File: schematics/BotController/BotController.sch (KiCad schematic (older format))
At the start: 53 parts, among them IC1 ATMEGA644A-P, P1 2x Serial, P10 Stepper Upperarm, P11 Stepper Shoulder, P12 POWER_IN, P13 PowerEnableIn, P17 PowerEnableOut, P2 Herkulex Servo, P28 Power Stepper, P3 Encoder Socket 0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

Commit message: resorted
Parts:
- added C?: 100nF, symbol C
- C11: value 100uF -> 2200uF
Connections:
- wire segments 217 -> 290
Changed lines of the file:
@@
 P 4750 10450
 F 0 "C11" H 4775 10550 50  0000 L CNN
-F 1 "100uF" H 4775 10350 50  0000 L CNN
+F 1 "2200uF" H 4775 10350 50  0000 L CNN
 F 2 "Capacitors_ThroughHole:C_Radial_D7.5_L11.2_P2.5" H 4788 10300 50  0001 C CNN
 F 3 "" H 4750 10450 50  0000 C CNN
@@
 	2250 7150 2250 7350
 Wire Wire Line
-	1000 7150 2250 7150
+	1000 7150 2050 7150
+Wire Wire Line
+	2050 7150 2250 7150
 Wire Wire Line
 	2050 7800 2050 7650
@@
 Connection ~ 2050 7150
 Wire Wire Line
-	9900 2700 9900 6350
+	9900 2700 9900 6200
+Wire Wire Line
+	9900 6200 9900 6350
 Wire Wire Line
 	9400 1700 9400 4000
@@
 Connection ~ 3050 1700
 Wire Wire Line
-	3050 1700 3050 7300
+	3050 1700 3050 7150
+Wire Wire Line
+	3050 7150 3050 7300
 Connection ~ 2250 7800
 Connection ~ 2050 7800
 Wire Wire Line
-	950  7800 3900 7800
+	950  7800 1200 7800
+Wire Wire Line
+	1200 7800 1750 7800
+Wire Wire Line
+	1750 7800 2050 7800
+Wire Wire Line
+	2050 7800 2250 7800
+Wire Wire Line
+	2250 7800 2650 7800
+Wire Wire Line
+	2650 7800 3050 7800
+Wire Wire Line
+	3050 7800 3900 7800
 Wire Wire Line
 	7350 6200 7350 6550
@@
 	9400 6200 9400 4300
 Wire Wire Line
-	6050 4200 9400 4200
-Wire Wire Line
-	6050 4100 9400 4100
+	6050 4200 8500 4200
+Wire Wire Line
+	8500 4200 9150 4200
+Wire Wire Line
+	9150 4200 9400 4200
+Wire Wire Line
+	6050 4100 8400 4100
+Wire Wire Line
+	8400 4100 8950 4100
+Wire Wire Line
+	8950 4100 9400 4100
 Wire Wire Line
 	7050 5300 7050 6550
@@
 	3700 6200 3700 5000
 Wire Wire Line
-	3700 1700 3700 4500
+	3700 1700 3700 3500
+Wire Wire Line
+	3700 3500 3700 4500
 Wire Wire Line
 	4050 3500 3700 3500
@@
 	6350 6200 6350 6550
 Wire Wire Line
-	1200 6200 11750 6200
+	1200 6200 1700 6200
+Wire Wire Line
+	1700 6200 2150 6200
+Wire Wire Line
+	2150 6200 2750 6200
+Wire Wire Line
+	2750 6200 3450 6200
+Wire Wire Line
+	3450 6200 3700 6200
+Wire Wire Line
+	3700 6200 4850 6200
+Wire Wire Line
+	4850 6200 5050 6200
+Wire Wire Line
+	5050 6200 6350 6200
+Wire Wire Line
+	6350 6200 7350 6200
+Wire Wire Line
+	7350 6200 8150 6200
+Wire Wire Line
+	8150 6200 9400 6200
+Wire Wire Line
+	9400 6200 9900 6200
+Wire Wire Line
+	9900 6200 10300 6200
+Wire Wire Line
+	10300 6200 10800 6200
+Wire Wire Line
+	10800 6200 11300 6200
+Wire Wire Line
+	11300 6200 11750 6200
 Wire Wire Line
 	7500 3900 6050 3900
@@
 	8150 4550 7850 4550
 Wire Wire Line
-	1200 1700 9400 1700
-Wire Wire Line
-	2750 2300 4050 2300
+	1200 1700 1700 1700
+Wire Wire Line
+	1700 1700 3050 1700
+Wire Wire Line
+	3050 1700 3450 1700
+Wire Wire Line
+	3450 1700 3700 1700
+Wire Wire Line
+	3700 1700 3850 1700
+Wire Wire Line
+	3850 1700 4050 1700
+Wire Wire Line
+	4050 1700 4850 1700
+Wire Wire Line
+	4850 1700 5050 1700
+Wire Wire Line
+	5050 1700 7050 1700
+Wire Wire Line
+	7050 1700 7850 1700
+Wire Wire Line
+	7850 1700 9150 1700
+Wire Wire Line
+	9150 1700 9400 1700
+Wire Wire Line
+	2750 2300 3850 2300
+Wire Wire Line
+	3850 2300 3950 2300
+Wire Wire Line
+	3950 2300 4050 2300
 Connection ~ 3850 1700
 Connection ~ 3850 2300
@@
 	4050 1700 4050 1800
 Wire Wire Line
-	1700 1700 7050 1700
+	1700 1700 3050 1700
+Wire Wire Line
+	3050 1700 3450 1700
+Wire Wire Line
+	3450 1700 3700 1700
+Wire Wire Line
+	3700 1700 3850 1700
+Wire Wire Line
+	3850 1700 4050 1700
+Wire Wire Line
+	4050 1700 4850 1700
+Wire Wire Line
+	4850 1700 5050 1700
+Wire Wire Line
+	5050 1700 7050 1700
 Connection ~ 1700 6200
 Wire Wire Line
-	1700 4200 1700 7800
+	1700 4200 1700 6200
+Wire Wire Line
+	1700 6200 1700 7800
 Wire Wire Line
 	8150 3700 8150 4550
@@
 	950  8600 1150 8600
 Wire Wire Line
-	1650 8400 10050 8400
+	1650 8400 7550 8400
+Wire Wire Line
+	7550 8400 10050 8400
 Wire Wire Line
 	10700 10800 10700 10500
@@
 Connection ~ 6900 10800
 Wire Wire Line
-	6900 9950 7450 9950
+	6900 9950 7200 9950
+Wire Wire Line
+	7200 9950 7450 9950
 Wire Wire Line
 	7200 9950 7200 10250
@@
 	7650 10600 7650 10350
 Wire Wire Line
-	6000 10200 8200 10200
+	6000 10200 7650 10200
+Wire Wire Line
+	7650 10200 8200 10200
 Wire Wire Line
 	7650 10250 7650 10200
@@
 Connection ~ 10700 10800
 Wire Wire Line
-	4750 9950 6100 9950
+	4750 9950 5050 9950
+Wire Wire Line
+	5050 9950 6100 9950
 Wire Wire Line
 	2000 9550 4750 9550
 Wire Wire Line
-	4750 8950 4750 10300
+	4750 8950 4750 9550
+Wire Wire Line
+	4750 9550 4750 9950
+Wire Wire Line
+	4750 9950 4750 10300
 Connection ~ 4750 9950
 Connection ~ 4750 9550
@@
 	4750 8950 5700 8950
 Wire Wire Line
-	5700 8700 5700 10450
+	5700 8700 5700 8950
+Wire Wire Line
+	5700 8950 5700 10200
+Wire Wire Line
+	5700 10200 5700 10450
 Wire Wire Line
 	950  8600 950  9450
@@
 	10700 9950 10700 10300
 Wire Wire Line
-	950  10800 11050 10800
+	950  10800 4750 10800
+Wire Wire Line
+	4750 10800 5050 10800
+Wire Wire Line
+	5050 10800 6500 10800
+Wire Wire Line
+	6500 10800 6850 10800
+Wire Wire Line
+	6850 10800 6900 10800
+Wire Wire Line
+	6900 10800 7200 10800
+Wire Wire Line
+	7200 10800 9450 10800
+Wire Wire Line
+	9450 10800 10000 10800
+Wire Wire Line
+	10000 10800 10350 10800
+Wire Wire Line
+	10350 10800 10700 10800
+Wire Wire Line
+	10700 10800 11050 10800
 Wire Wire Line
 	950  9550 1700 9550
@@
 	8200 10200 8200 10300
 Wire Wire Line
-	4750 9400 4750 9950
+	4750 9400 4750 9550
+Wire Wire Line
+	4750 9550 4750 9950
 Wire Wire Line
 	4750 9400 9050 9400
@@
 Connection ~ 9450 10800
 Wire Wire Line
-	9850 9400 10500 9400
+	9850 9400 10000 9400
+Wire Wire Line
+	10000 9400 10350 9400
+Wire Wire Line
+	10350 9400 10500 9400
 Wire Wire Line
 	10000 9400 10000 9500
@@
 	6400 5400 6050 5400
 NoConn ~ 6050 6550
+$Comp
+L C C?
+U 1 1 578BFFF7
+P 10350 10150
+F 0 "C?" H 10375 10250 50  0000 L CNN
+F 1 "100nF" H 10375 10050 50  0000 L CNN
+F 2 "" H 10388 10000 50  0000 C CNN
+F 3 "" H 10350 10150 50  0000 C CNN
+	1    10350 10150
+	1    0    0    -1
+$EndComp
+Wire Wire Line
+	10350 10000 10350 9400
+Connection ~ 10350 9400
+Wire Wire Line
+	10350 10300 10350 10800
+Connection ~ 10350 10800
 $EndSCHEMATC

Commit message: PCB angefangen
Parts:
- C6: renamed from C?; footprint (none) -> Capacitors_ThroughHole:C_Disc_D3_P2.5
- P6: footprint Connectors_Molex:Molex_KK_6410-03 -> Connect:bornier3
- R3, R4: value 1.5K -> 4.7K
- RV1: footprint Potentiometers:Potentiometer_Trimmer-Piher_PT15-V12-5_horizontal -> BotController:Potentiometer_Trimmer-ALPS-horizontal
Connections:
- wire segments 290 -> 218
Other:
- moved on the sheet: D2
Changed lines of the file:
@@
 P 9150 3800
 F 0 "R4" V 9230 3800 50  0000 C CNN
-F 1 "1.5K" V 9150 3800 50  0000 C CNN
+F 1 "4.7K" V 9150 3800 50  0000 C CNN
 F 2 "BotController:R4(7)" V 9080 3800 30  0001 C CNN
 F 3 "" H 9150 3800 30  0000 C CNN
@@
 P 8950 3800
 F 0 "R3" V 9030 3800 50  0000 C CNN
-F 1 "1.5K" V 8950 3800 50  0000 C CNN
+F 1 "4.7K" V 8950 3800 50  0000 C CNN
 F 2 "BotController:R4(8)" V 8880 3800 30  0001 C CNN
 F 3 "" H 8950 3800 30  0000 C CNN
@@
 F 0 "RV1" H 3700 4650 50  0000 C CNN
 F 1 "10K" H 3700 4750 50  0000 C CNN
-F 2 "Potentiometers:Potentiometer_Trimmer-Piher_PT15-V12-5_horizontal" H 3700 4750 60  0001 C CNN
+F 2 "BotController:Potentiometer_Trimmer-ALPS-horizontal" H 3700 4750 60  0001 C CNN
 F 3 "" H 3700 4750 60  0000 C CNN
 	1    3700 4750
@@
 F 0 "P6" H 750 7900 50  0000 C CNN
 F 1 "Power In uC Servo" V 850 7700 50  0000 C CNN
-F 2 "Connectors_Molex:Molex_KK_6410-03" H 750 7700 50  0001 C CNN
+F 2 "Connect:bornier3" H 750 7700 50  0001 C CNN
 F 3 "" H 750 7700 50  0000 C CNN
 	1    750  7700
@@
 L LED D2
 U 1 1 577C1DF8
-P 7050 2050
-F 0 "D2" H 7050 2150 50  0000 C CNN
-F 1 "LED" H 7050 1950 50  0000 C CNN
-F 2 "LEDs:LED-3MM" H 7050 2050 50  0001 C CNN
-F 3 "" H 7050 2050 50  0000 C CNN
-	1    7050 2050
-	0    1    1    0
+P 6900 4500
+F 0 "D2" H 6900 4600 50  0000 C CNN
+F 1 "LED" H 6900 4400 50  0000 C CNN
+F 2 "LEDs:LED-3MM" H 6900 4500 50  0001 C CNN
+F 3 "" H 6900 4500 50  0000 C CNN
+	1    6900 4500
+	0    -1   -1   0
 $EndComp
 $Comp
@@
 	2250 7150 2250 7350
 Wire Wire Line
-	1000 7150 2050 7150
-Wire Wire Line
-	2050 7150 2250 7150
+	1000 7150 2250 7150
 Wire Wire Line
 	2050 7800 2050 7650
@@
 Connection ~ 2050 7150
 Wire Wire Line
-	9900 2700 9900 6200
-Wire Wire Line
-	9900 6200 9900 6350
+	9900 2700 9900 6350
 Wire Wire Line
 	9400 1700 9400 4000
@@
 Wire Wire Line
 	6050 2300 6100 2300
-Wire Wire Line
-	7050 3400 6550 3400
 Wire Wire Line
 	6050 3400 6250 3400
@@
 Connection ~ 3050 1700
 Wire Wire Line
-	3050 1700 3050 7150
-Wire Wire Line
-	3050 7150 3050 7300
+	3050 1700 3050 7300
 Connection ~ 2250 7800
 Connection ~ 2050 7800
 Wire Wire Line
-	950  7800 1200 7800
-Wire Wire Line
-	1200 7800 1750 7800
-Wire Wire Line
-	1750 7800 2050 7800
-Wire Wire Line
-	2050 7800 2250 7800
-Wire Wire Line
-	2250 7800 2650 7800
-Wire Wire Line
-	2650 7800 3050 7800
-Wire Wire Line
-	3050 7800 3900 7800
-Wire Wire Line
 	7350 6200 7350 6550
 Connection ~ 7350 6200
@@
 	9400 6200 9400 4300
 Wire Wire Line
-	6050 4200 8500 4200
-Wire Wire Line
-	8500 4200 9150 4200
-Wire Wire Line
-	9150 4200 9400 4200
-Wire Wire Line
-	6050 4100 8400 4100
-Wire Wire Line
-	8400 4100 8950 4100
-Wire Wire Line
-	8950 4100 9400 4100
+	6050 4200 9400 4200
+Wire Wire Line
+	6050 4100 9400 4100
 Wire Wire Line
 	7050 5300 7050 6550
@@
 	3700 6200 3700 5000
 Wire Wire Line
-	3700 1700 3700 3500
-Wire Wire Line
-	3700 3500 3700 4500
+	3700 1700 3700 4500
 Wire Wire Line
 	4050 3500 3700 3500
-Connection ~ 7050 1700
-Wire Wire Line
-	7050 1700 7050 1850
-Wire Wire Line
-	7050 2250 7050 3400
 Wire Wire Line
 	6150 5100 6150 6550
@@
 	6350 6200 6350 6550
 Wire Wire Line
-	1200 6200 1700 6200
-Wire Wire Line
-	1700 6200 2150 6200
-Wire Wire Line
-	2150 6200 2750 6200
-Wire Wire Line
-	2750 6200 3450 6200
-Wire Wire Line
-	3450 6200 3700 6200
-Wire Wire Line
-	3700 6200 4850 6200
-Wire Wire Line
-	4850 6200 5050 6200
-Wire Wire Line
-	5050 6200 6350 6200
-Wire Wire Line
-	6350 6200 7350 6200
-Wire Wire Line
-	7350 6200 8150 6200
-Wire Wire Line
-	8150 6200 9400 6200
-Wire Wire Line
-	9400 6200 9900 6200
-Wire Wire Line
-	9900 6200 10300 6200
-Wire Wire Line
-	10300 6200 10800 6200
-Wire Wire Line
-	10800 6200 11300 6200
-Wire Wire Line
-	11300 6200 11750 6200
+	1200 6200 11750 6200
 Wire Wire Line
 	7500 3900 6050 3900
@@
 	8150 4550 7850 4550
 Wire Wire Line
-	1200 1700 1700 1700
-Wire Wire Line
-	1700 1700 3050 1700
-Wire Wire Line
-	3050 1700 3450 1700
-Wire Wire Line
-	3450 1700 3700 1700
-Wire Wire Line
-	3700 1700 3850 1700
-Wire Wire Line
-	3850 1700 4050 1700
-Wire Wire Line
-	4050 1700 4850 1700
-Wire Wire Line
-	4850 1700 5050 1700
-Wire Wire Line
-	5050 1700 7050 1700
-Wire Wire Line
-	7050 1700 7850 1700
-Wire Wire Line
-	7850 1700 9150 1700
-Wire Wire Line
-	9150 1700 9400 1700
-Wire Wire Line
-	2750 2300 3850 2300
-Wire Wire Line
-	3850 2300 3950 2300
-Wire Wire Line
-	3950 2300 4050 2300
+	1200 1700 9400 1700
+Wire Wire Line
+	2750 2300 4050 2300
 Connection ~ 3850 1700
 Connection ~ 3850 2300
@@
 	4050 1700 4050 1800
 Wire Wire Line
-	1700 1700 3050 1700
-Wire Wire Line
-	3050 1700 3450 1700
-Wire Wire Line
-	3450 1700 3700 1700
-Wire Wire Line
-	3700 1700 3850 1700
-Wire Wire Line
-	3850 1700 4050 1700
-Wire Wire Line
-	4050 1700 4850 1700
-Wire Wire Line
-	4850 1700 5050 1700
-Wire Wire Line
-	5050 1700 7050 1700
+	1700 1700 7050 1700
 Connection ~ 1700 6200
-Wire Wire Line
-	1700 4200 1700 6200
-Wire Wire Line
-	1700 6200 1700 7800
 Wire Wire Line
 	8150 3700 8150 4550
@@
 	950  8600 1150 8600
 Wire Wire Line
-	1650 8400 7550 8400
-Wire Wire Line
-	7550 8400 10050 8400
+	1650 8400 10050 8400
 Wire Wire Line
 	10700 10800 10700 10500
@@
 Connection ~ 6900 10800
 Wire Wire Line
-	6900 9950 7200 9950
-Wire Wire Line
-	7200 9950 7450 9950
+	6900 9950 7450 9950
 Wire Wire Line
 	7200 9950 7200 10250
@@
 	7650 10600 7650 10350
 Wire Wire Line
-	6000 10200 7650 10200
-Wire Wire Line
-	7650 10200 8200 10200
+	6000 10200 8200 10200
 Wire Wire Line
 	7650 10250 7650 10200
@@
 Connection ~ 10700 10800
 Wire Wire Line
-	4750 9950 5050 9950
-Wire Wire Line
-	5050 9950 6100 9950
+	4750 9950 6100 9950
 Wire Wire Line
 	2000 9550 4750 9550
 Wire Wire Line
-	4750 8950 4750 9550
-Wire Wire Line
-	4750 9550 4750 9950
-Wire Wire Line
-	4750 9950 4750 10300
+	4750 8950 4750 10300
 Connection ~ 4750 9950
 Connection ~ 4750 9550
@@
 	4750 8950 5700 8950
 Wire Wire Line
-	5700 8700 5700 8950
-Wire Wire Line
-	5700 8950 5700 10200
-Wire Wire Line
-	5700 10200 5700 10450
+	5700 8700 5700 10450
 Wire Wire Line
 	950  8600 950  9450
@@
 	10700 9950 10700 10300
 Wire Wire Line
-	950  10800 4750 10800
-Wire Wire Line
-	4750 10800 5050 10800
-Wire Wire Line
-	5050 10800 6500 10800
-Wire Wire Line
-	6500 10800 6850 10800
-Wire Wire Line
-	6850 10800 6900 10800
-Wire Wire Line
-	6900 10800 7200 10800
-Wire Wire Line
-	7200 10800 9450 10800
-Wire Wire Line
-	9450 10800 10000 10800
-Wire Wire Line
-	10000 10800 10350 10800
-Wire Wire Line
-	10350 10800 10700 10800
-Wire Wire Line
-	10700 10800 11050 10800
+	950  10800 11050 10800
 Wire Wire Line
 	950  9550 1700 9550
@@
 	8200 10200 8200 10300
 Wire Wire Line
-	4750 9400 4750 9550
-Wire Wire Line
-	4750 9550 4750 9950
+	4750 9400 4750 9950
 Wire Wire Line
 	4750 9400 9050 9400
@@
 Connection ~ 9450 10800
 Wire Wire Line
-	9850 9400 10000 9400
-Wire Wire Line
-	10000 9400 10350 9400
-Wire Wire Line
-	10350 9400 10500 9400
+	9850 9400 10500 9400
 Wire Wire Line
 	10000 9400 10000 9500
@@
 Wire Wire Line
 	4050 2900 4050 3100
-Wire Wire Line
-	1700 7800 1750 7800
-Connection ~ 1750 7800
 Connection ~ 5700 8950
 Wire Wire Line
@@
 NoConn ~ 6050 6550
 $Comp
-L C C?
+L C C6
 U 1 1 578BFFF7
 P 10350 10150
-F 0 "C?" H 10375 10250 50  0000 L CNN
+F 0 "C6" H 10375 10250 50  0000 L CNN
 F 1 "100nF" H 10375 10050 50  0000 L CNN
-F 2 "" H 10388 10000 50  0000 C CNN
+F 2 "Capacitors_ThroughHole:C_Disc_D3_P2.5" H 10388 10000 50  0001 C CNN
 F 3 "" H 10350 10150 50  0000 C CNN
 	1    10350 10150
@@
 	10350 10300 10350 10800
 Connection ~ 10350 10800
+Wire Wire Line
+	6900 3400 6900 4300
+Wire Wire Line
+	6550 3400 6900 3400
+Wire Wire Line
+	6900 4700 6900 6200
+Connection ~ 6900 6200
+Wire Wire Line
+	950  7800 3900 7800
+Wire Wire Line
+	1700 4200 1700 7800
+Connection ~ 1700 7800
 $EndSCHEMATC

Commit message: no message
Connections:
- wire segments 218 -> 219
- no-connect marks 11 -> 10
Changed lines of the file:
@@
 Wire Wire Line
 	6400 5400 6050 5400
-NoConn ~ 6050 6550
 $Comp
 L C C6
@@
 	1700 4200 1700 7800
 Connection ~ 1700 7800
+Wire Wire Line
+	6050 6550 6050 6200
+Connection ~ 6050 6200
 $EndSCHEMATC

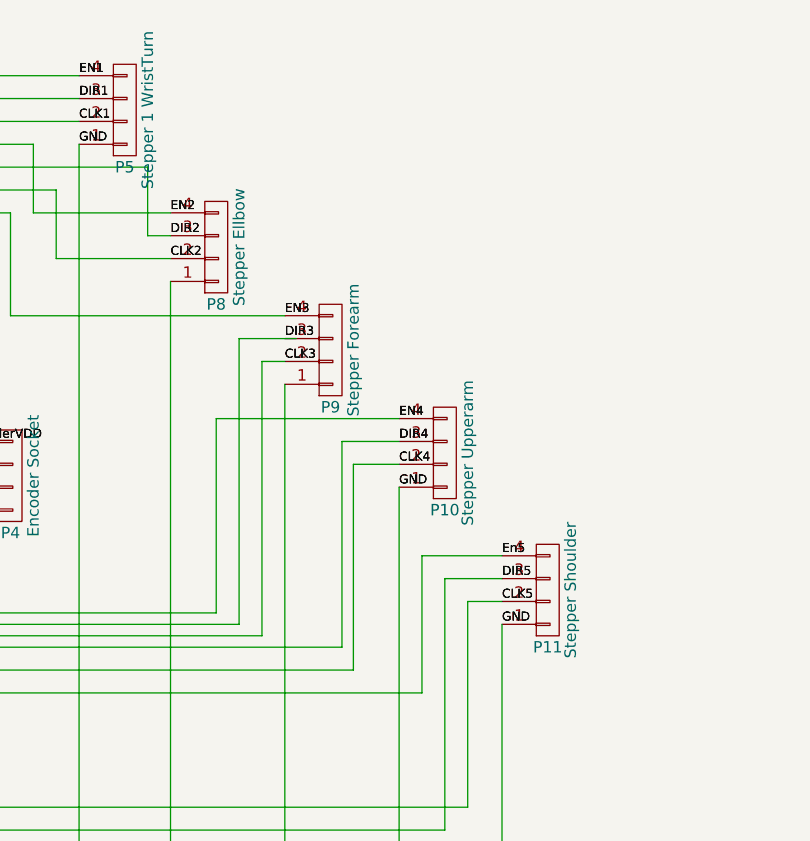
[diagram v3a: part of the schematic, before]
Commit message: Stecker umbenannt
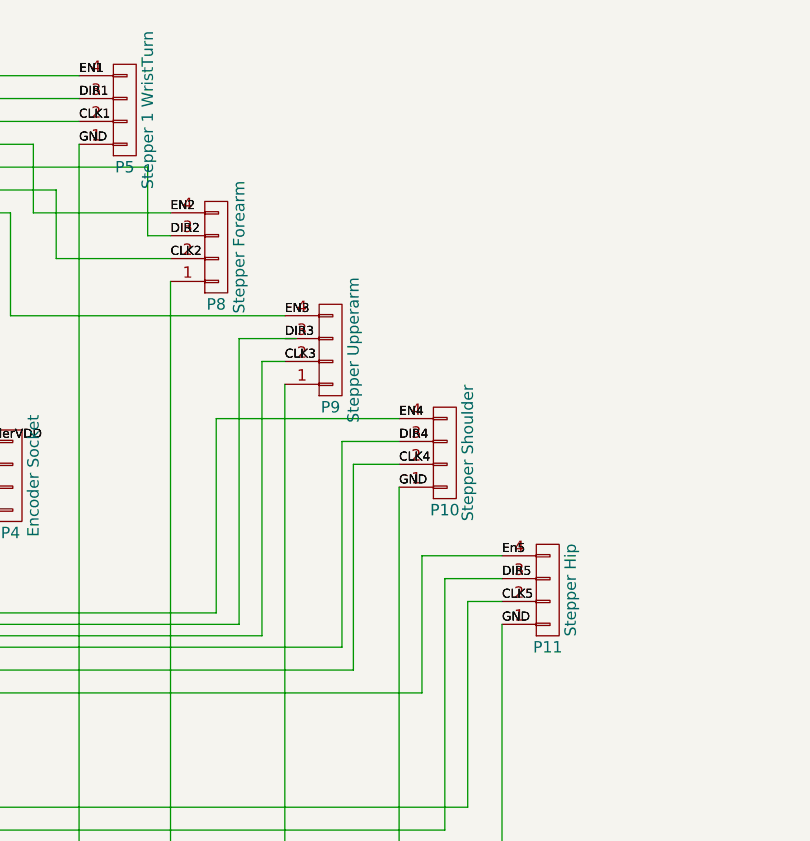
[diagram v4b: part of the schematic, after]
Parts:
- P10: value Stepper Upperarm -> Stepper Shoulder
- P11: value Stepper Shoulder -> Stepper Hip
- P8: value Stepper Ellbow -> Stepper Forearm
- P9: value Stepper Forearm -> Stepper Upperarm
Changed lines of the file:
@@
 P 11950 4650
 F 0 "P11" H 11950 4900 50  0000 C CNN
-F 1 "Stepper Shoulder" V 12050 4650 50  0000 C CNN
+F 1 "Stepper Hip" V 12050 4650 50  0000 C CNN
 F 2 "Connectors_Molex:Molex_KK_6410-04" H 11950 4650 60  0001 C CNN
 F 3 "" H 11950 4650 60  0000 C CNN
@@
 P 11500 4050
 F 0 "P10" H 11500 4300 50  0000 C CNN
-F 1 "Stepper Upperarm" V 11600 4050 50  0000 C CNN
+F 1 "Stepper Shoulder" V 11600 4050 50  0000 C CNN
 F 2 "Connectors_Molex:Molex_KK_6410-04" H 11500 4050 60  0001 C CNN
 F 3 "" H 11500 4050 60  0000 C CNN
@@
 P 11000 3600
 F 0 "P9" H 11000 3850 50  0000 C CNN
-F 1 "Stepper Forearm" V 11100 3600 50  0000 C CNN
+F 1 "Stepper Upperarm" V 11100 3600 50  0000 C CNN
 F 2 "Connectors_Molex:Molex_KK_6410-04" H 11000 3600 60  0001 C CNN
 F 3 "" H 11000 3600 60  0000 C CNN
@@
 P 10500 3150
 F 0 "P8" H 10500 3400 50  0000 C CNN
-F 1 "Stepper Ellbow" V 10600 3150 50  0000 C CNN
+F 1 "Stepper Forearm" V 10600 3150 50  0000 C CNN
 F 2 "Connectors_Molex:Molex_KK_6410-04" H 10500 3150 60  0001 C CNN
 F 3 "" H 10500 3150 60  0000 C CNN

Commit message: no message
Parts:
- added P14: Power Stepper 2, Connect:bornier2, symbol CONN_01X02
- added P15: Power Stepper 3, Connect:bornier2, symbol CONN_01X02
- added P16: Power Stepper 4, Connect:bornier2, symbol CONN_01X02
- added P18: Power Stepper 5, Connect:bornier2, symbol CONN_01X02
- P28: value Power Stepper -> Power Stepper 1
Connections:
- wire segments 219 -> 229
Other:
- moved on the sheet: C11, C12, C13, C14, C3, C4, C5, C6, D1, D10, P17, P28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

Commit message: Wochenende
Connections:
- wire segments 229 -> 306

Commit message: Power PCB works!
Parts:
- removed Q1, Q2: Q_NPN_BCE, TO_SOT_Packages_THT:TO-92_Inline_Wide, symbol Q_NPN_BCE
- added P19: ODroid Power, Connect:bornier2, symbol CONN_01X02
- added Q1, Q2: BC237, TO_SOT_Packages_THT:TO-92_Molded_Wide, symbol BC237
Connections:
- net 5V: now also P19.1 (P1)
- net GNDPWR: now also P19.2 (P2), Q1.3 (E), Q2.3 (E)
- net at D10.2 (A), REL2.1: now also Q2.1 (C)
- net at D1.2 (A), REL1.1: now also Q1.1 (C)
- net at R10.1: now also Q2.2 (B)
- net at R8.1: now also Q1.2 (B)
- no-connect marks 10 -> 9

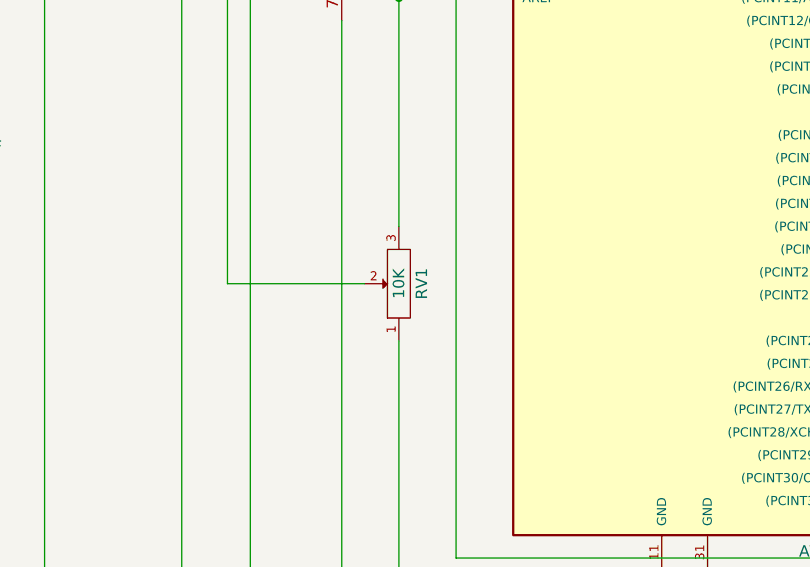
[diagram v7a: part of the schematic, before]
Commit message: added power supply to the housing
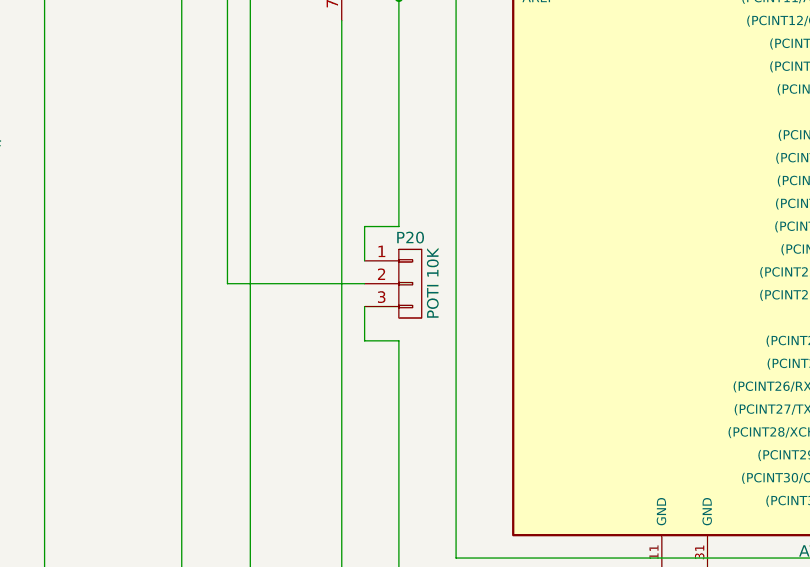
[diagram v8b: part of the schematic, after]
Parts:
- removed RV1: 10K, BotController:Potentiometer_Trimmer-ALPS-horizontal, symbol POT
- added P20: POTI 10K, Connectors_Molex:Molex_KK_6410-03, symbol CONN_01X03
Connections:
- net +5V: now also P20.1 (P1)
- net GNDPWR: now also P20.3 (P3)
- net at IC1.40 ((PCINT0/ADC0)PA0): now also P20.2 (P2)
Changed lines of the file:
@@
-$EndComp
-$Comp
-L POT RV1
-U 1 1 572524E5
-P 3700 4750
-F 0 "RV1" H 3700 4650 50  0000 C CNN
-F 1 "10K" H 3700 4750 50  0000 C CNN
-F 2 "BotController:Potentiometer_Trimmer-ALPS-horizontal" H 3700 4750 60  0001 C CNN
-F 3 "" H 3700 4750 60  0000 C CNN
-	1    3700 4750
-	0    -1   -1   0
 $EndComp
 $Comp
@@
 	1    0    0    -1
 $EndComp
+$Comp
+L CONN_01X03 P20
+U 1 1 585035A0
+P 3750 4750
+F 0 "P20" H 3750 4950 50  0000 C CNN
+F 1 "POTI 10K" V 3850 4750 50  0000 C CNN
+F 2 "Connectors_Molex:Molex_KK_6410-03" H 3750 4750 50  0001 C CNN
+F 3 "" H 3750 4750 50  0000 C CNN
+	1    3750 4750
+	1    0    0    -1
+$EndComp
+Wire Wire Line
+	3700 4500 3550 4500
+Wire Wire Line
+	3550 4500 3550 4650
+Wire Wire Line
+	3550 4850 3550 5000
+Wire Wire Line
+	3550 5000 3700 5000
 $EndSCHEMATC
